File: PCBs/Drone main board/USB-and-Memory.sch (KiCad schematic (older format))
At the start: 36 parts, among them J601 UJ2-MBH-1-SMT-TR, U601 93LCxxBxxOT, U602 FT232H, U603 MT25QL512ABB8ESF-0SIT, U604 W25Q128JVS, Y601 12MHz

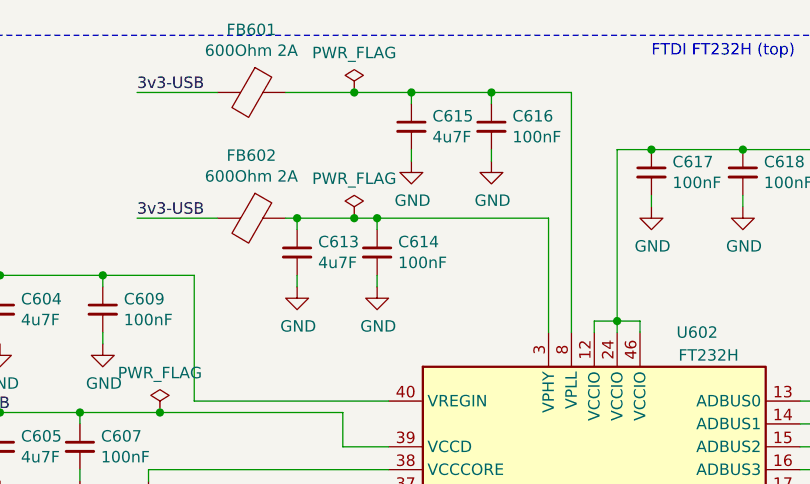
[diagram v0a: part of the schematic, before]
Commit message: Some cleanup, and PCB antenna removal.
Last edits before asking for reddit feedback.

Signed-off-by: Eldalote.Electronics <Eldalote.Electronics@gmail.com>
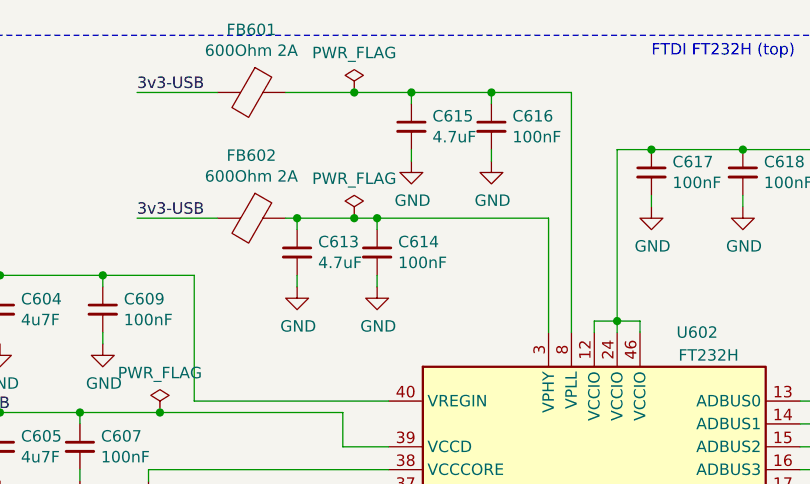
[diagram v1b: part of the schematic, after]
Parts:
- C613, C615: value 4u7F -> 4.7uF
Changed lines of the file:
@@
 P 2300 1500
 F 0 "C613" H 2392 1546 50  0000 L CNN
-F 1 "4u7F" H 2392 1455 50  0000 L CNN
+F 1 "4.7uF" H 2392 1455 50  0000 L CNN
 F 2 "Capacitor_SMD:C_0402_1005Metric" H 2300 1500 50  0001 C CNN
 F 3 "~" H 2300 1500 50  0001 C CNN
@@
 P 2800 950
 F 0 "C615" H 2892 996 50  0000 L CNN
-F 1 "4u7F" H 2892 905 50  0000 L CNN
+F 1 "4.7uF" H 2892 905 50  0000 L CNN
 F 2 "Capacitor_SMD:C_0402_1005Metric" H 2800 950 50  0001 C CNN
 F 3 "~" H 2800 950 50  0001 C CNN

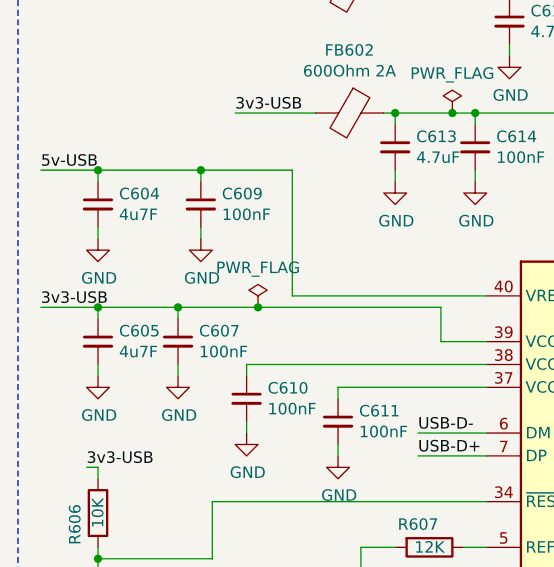
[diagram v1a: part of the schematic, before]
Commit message: Added PDFs of schematics. Corrected a few value labels in drone schematic.
Signed-off-by: Eldalote.Electronics <Eldalote.Electronics@gmail.com>
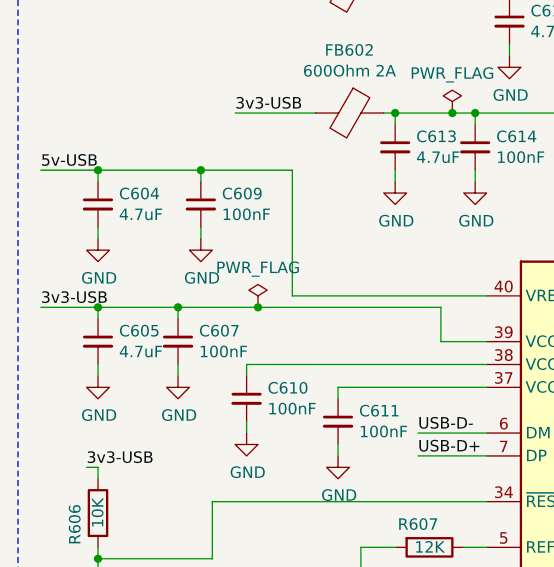
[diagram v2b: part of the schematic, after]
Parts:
- C604, C605: value 4u7F -> 4.7uF
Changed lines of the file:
@@
 P 1000 1750
 F 0 "C604" H 1092 1796 50  0000 L CNN
-F 1 "4u7F" H 1092 1705 50  0000 L CNN
+F 1 "4.7uF" H 1092 1705 50  0000 L CNN
 F 2 "Capacitor_SMD:C_0402_1005Metric" H 1000 1750 50  0001 C CNN
 F 3 "~" H 1000 1750 50  0001 C CNN
@@
 P 1000 2350
 F 0 "C605" H 1092 2396 50  0000 L CNN
-F 1 "4u7F" H 1092 2305 50  0000 L CNN
+F 1 "4.7uF" H 1092 2305 50  0000 L CNN
 F 2 "Capacitor_SMD:C_0402_1005Metric" H 1000 2350 50  0001 C CNN
 F 3 "~" H 1000 2350 50  0001 C CNN

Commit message: Lots of work to check every component, add Manufacturers number (instead of LCSC or digikey and mouser numbers)
Changed to USB-C connector, almost done with that sheet. Components checked, need to redo Sheet IO

Signed-off-by: Eldalote.Electronics <Eldalote.Electronics@gmail.com>
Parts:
- removed J601: UJ2-MBH-1-SMT-TR, digikey-footprints:USB_Mini_B_Female_UJ2-MBH-1-SMT-TR, symbol dk_USB-DVI-HDMI-Connectors:UJ2-MBH-1-SMT-TR
- added J601: DX07S016JA1R1500, Eldalote-footprints:JAE_DX07S016JA1R1500, symbol Eldalote-General:DX07S016JA1R1500
- added R608, R609: 5k1, Resistor_SMD:R_0402_1005Metric, symbol Device:R
- C601, C603: footprint Capacitor_SMD:C_0805_2012Metric_Pad1.15x1.40mm_HandSolder -> Capacitor_SMD:C_0402_1005Metric; DigiKey 1276-1099-1-ND -> (none); MfNr (none) -> CL05B104KO5NNNC; Mouser 187-CL21B104KACNNNC -> (none)
- C602, C607, C609, C610, C611, C614, C616, C617, C618, C619: LCSC C1525 -> (none); MfNr (none) -> CL05B104KO5NNNC
- C604, C605, C613, C615: LCSC C23733 -> (none); MfNr (none) -> CL05A475MP5NRN
- C606: LCSC C15195 -> (none); MfNr (none) -> CL05B103KB5NNN
- C608, C612: value 33pF -> 27pF; LCSC C1562 -> (none); MfNr (none) -> CL05C270JB5NNN
- C620: LCSC C15195 -> (none); MfNr (none) -> CL05B103KB5NNNC
- FB601, FB602, FB603: footprint Resistor_SMD:R_0805_2012Metric_Pad1.15x1.40mm_HandSolder -> Resistor_SMD:R_0805_2012Metric; DigiKey 1934-1487-1-ND -> (none); MfNr (none) -> 2508056017Y2; Mouser 623-2508056017Y2 -> (none)
- R601, R603, R604: footprint Resistor_SMD:R_0805_2012Metric_Pad1.15x1.40mm_HandSolder -> Resistor_SMD:R_0402_1005Metric; DigiKey 311-10.0KCRCT-ND -> (none); MfNr (none) -> RC0402FR-0710KL; Mouser 603-RC0805FR-0710KL -> (none)
- R602: footprint Resistor_SMD:R_0805_2012Metric_Pad1.15x1.40mm_HandSolder -> Resistor_SMD:R_0402_1005Metric; DigiKey 311-2.00KCRCT-ND -> (none); MfNr (none) -> RC0402FR-072KL; Mouser 603-RC0805FR-072KL -> (none)
- R605: footprint Resistor_SMD:R_0805_2012Metric_Pad1.15x1.40mm_HandSolder -> Resistor_SMD:R_0402_1005Metric; DigiKey 2019-RK73H2ATTD24R9FCT-ND -> (none); MfNr (none) -> RC0402FR-0724R9L; Mouser 660-RK73H2ATTD24R9F -> (none)
- R606: LCSC C25744 -> (none); MfNr (none) -> RC0402FR-0710KL
- R607: LCSC C25752 -> (none); MfNr (none) -> ERJ-2RKF1202X
- U601: DigiKey 93LC56BT-I/OTCT-ND -> (none); MfNr (none) -> 93LC56BT-I/OT; Mouser 579-93LC56BT-I/OT -> (none)
- U602: DigiKey 768-1101-1-ND -> (none); LCSC Extended and expensive -> (none); MfNr (none) -> FT232HL; Mouser 895-FT232HL-REEL -> (none)
- U603: DigiKey 557-1651-ND -> (none); Manufacturer_Part_Number MT25QL512ABB8ESF-0SIT -> (none); MfNr (none) -> MT25QL512ABB8ESF-0SIT; Mouser 340-278183-TRAY -> (none); Mouser Part Number 340-278183-TRAY -> (none); Mouser Price/Stock https://www.mouser.co.uk/ProductDetail/Micron/MT25QL512ABB8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 -> (none)
- U604: LCSC C97521 -> (none); MfNr (none) -> W25Q128JVSIM
- Y601: footprint Crystal:Crystal_SMD_3225-4Pin_3.2x2.5mm -> Eldalote-footprints:Crystal_HC-49_US; symbol Device:Crystal_GND24 -> Device:Crystal; LCSC C9002 -> ABLS2-12.000MHZ-D4Y-T
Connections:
- net GND: now also J601.1 (GND), J601.12 (GND), J601.S1 (SHIELD), J601.S2 (SHIELD), J601.S3 (SHIELD), J601.S4 (SHIELD), J601.S5 (SHIELD), J601.S6 (SHIELD), R608.2, R609.2; no longer Y601.2, Y601.4
- net USB-D+: now also J601.6 (D+), J601.7 (D+)
- net USB-D-: now also J601.5 (D-), J601.8 (D-)
- net at C612.1, U602.2 (XCSO): now also Y601.2; no longer Y601.3
- net VBUS: now reaches C620.1, FB603.2
- net VBUS: now also J601.11 (VBUS), J601.2 (VBUS)
- new net: J601.3 (CC1), R608.1
- new net: J601.9 (CC2), R609.1
- no-connect marks 1 -> 0
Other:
- note added: "USB-C (2.0) connector (Top)"
- note removed: "USB-Mini connector (Top)"
- moved on the sheet: C604, C605, C606, C607, C608, C609, C610, C611, C612, C613, C614, C615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

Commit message: Reworking and checking up to sensors page on main board. Added some datasheets to project
Signed-off-by: Eldalote.Electronics <Eldalote.Electronics@gmail.com>
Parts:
- added D601: ESD7004, Package_DFN_QFN:Diodes_UDFN-10_1.0x2.5mm_P0.5mm, symbol Eldalote-General:ESD7004
- C608, C612: value 27pF -> 8.2pF; MfNr CL05C270JB5NNN -> CC0402CRNPO9BN8R2
- Y601: footprint Eldalote-footprints:Crystal_HC-49_US -> Eldalote-footprints:Crystal NDK 3.2x2.5; symbol Device:Crystal -> Device:Crystal_GND24; LCSC ABLS2-12.000MHZ-D4Y-T -> (none); MfNr (none) -> NX3225SA-12.000M-STD-CSR-1
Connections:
- net GND: now also Y601.2, Y601.4, D601.3, D601.8 (GND)
- net USB-D+: now also D601.4, D601.7 (NC)
- net USB-D-: now also D601.2, D601.9 (NC)
- net VBUS: now also D601.1, D601.10 (NC)
- net at C612.1, U602.2 (XCSO): now also Y601.3; no longer Y601.2
- new net: D601.5, D601.6 (NC)
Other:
- note added: "USB ESD Protection (Top)"
- moved on the sheet: C620, FB603, J601, R608, R609

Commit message: Minor PCB work
Signed-off-by: Eldalote.Electronics <Eldalote.Electronics@gmail.com>
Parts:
- FB601, FB602, FB603: value 600Ohm 2A -> 600Ohm 1.3A; footprint Resistor_SMD:R_0805_2012Metric -> Resistor_SMD:R_0603_1608Metric; MfNr 2508056017Y2 -> BLM18KG601SH1D
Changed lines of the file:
@@
 P 4800 850
 F 0 "FB601" V 4526 850 50  0000 C CNN
-F 1 "600Ohm 2A" V 4617 850 50  0000 C CNN
-F 2 "Resistor_SMD:R_0805_2012Metric" V 4730 850 50  0001 C CNN
+F 1 "600Ohm 1.3A" V 4617 850 50  0000 C CNN
+F 2 "Resistor_SMD:R_0603_1608Metric" V 4730 850 50  0001 C CNN
 F 3 "~" H 4800 850 50  0001 C CNN
-F 4 "2508056017Y2" V 4800 850 50  0001 C CNN "MfNr"
+F 4 "BLM18KG601SH1D" V 4800 850 50  0001 C CNN "MfNr"
 	1    4800 850
 	0    1    1    0
@@
 P 4800 1400
 F 0 "FB602" V 4526 1400 50  0000 C CNN
-F 1 "600Ohm 2A" V 4617 1400 50  0000 C CNN
-F 2 "Resistor_SMD:R_0805_2012Metric" V 4730 1400 50  0001 C CNN
+F 1 "600Ohm 1.3A" V 4617 1400 50  0000 C CNN
+F 2 "Resistor_SMD:R_0603_1608Metric" V 4730 1400 50  0001 C CNN
 F 3 "~" H 4800 1400 50  0001 C CNN
-F 4 "2508056017Y2" V 4800 1400 50  0001 C CNN "MfNr"
+F 4 "BLM18KG601SH1D" V 4800 1400 50  0001 C CNN "MfNr"
 	1    4800 1400
 	0    1    1    0
@@
 P 7000 5900
 F 0 "FB603" V 6726 5900 50  0000 C CNN
-F 1 "600Ohm 2A" V 6817 5900 50  0000 C CNN
-F 2 "Resistor_SMD:R_0805_2012Metric" V 6930 5900 50  0001 C CNN
+F 1 "600Ohm 1.3A" V 6817 5900 50  0000 C CNN
+F 2 "Resistor_SMD:R_0603_1608Metric" V 6930 5900 50  0001 C CNN
 F 3 "~" H 7000 5900 50  0001 C CNN
-F 4 "2508056017Y2" V 7000 5900 50  0001 C CNN "MfNr"
+F 4 "BLM18KG601SH1D" V 7000 5900 50  0001 C CNN "MfNr"
 	1    7000 5900
 	0    1    1    0
